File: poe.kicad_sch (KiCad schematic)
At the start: 57 parts, among them Q1 SI7430DP, Q2 MMBTA06LT1G, U1 MP8008, U10 MagJack-A70-112-331N126, U2 FOD817S, U3 750310744, U6 TL432DBZ, U7 TPD4EUSB30, U8 TPD4EUSB30

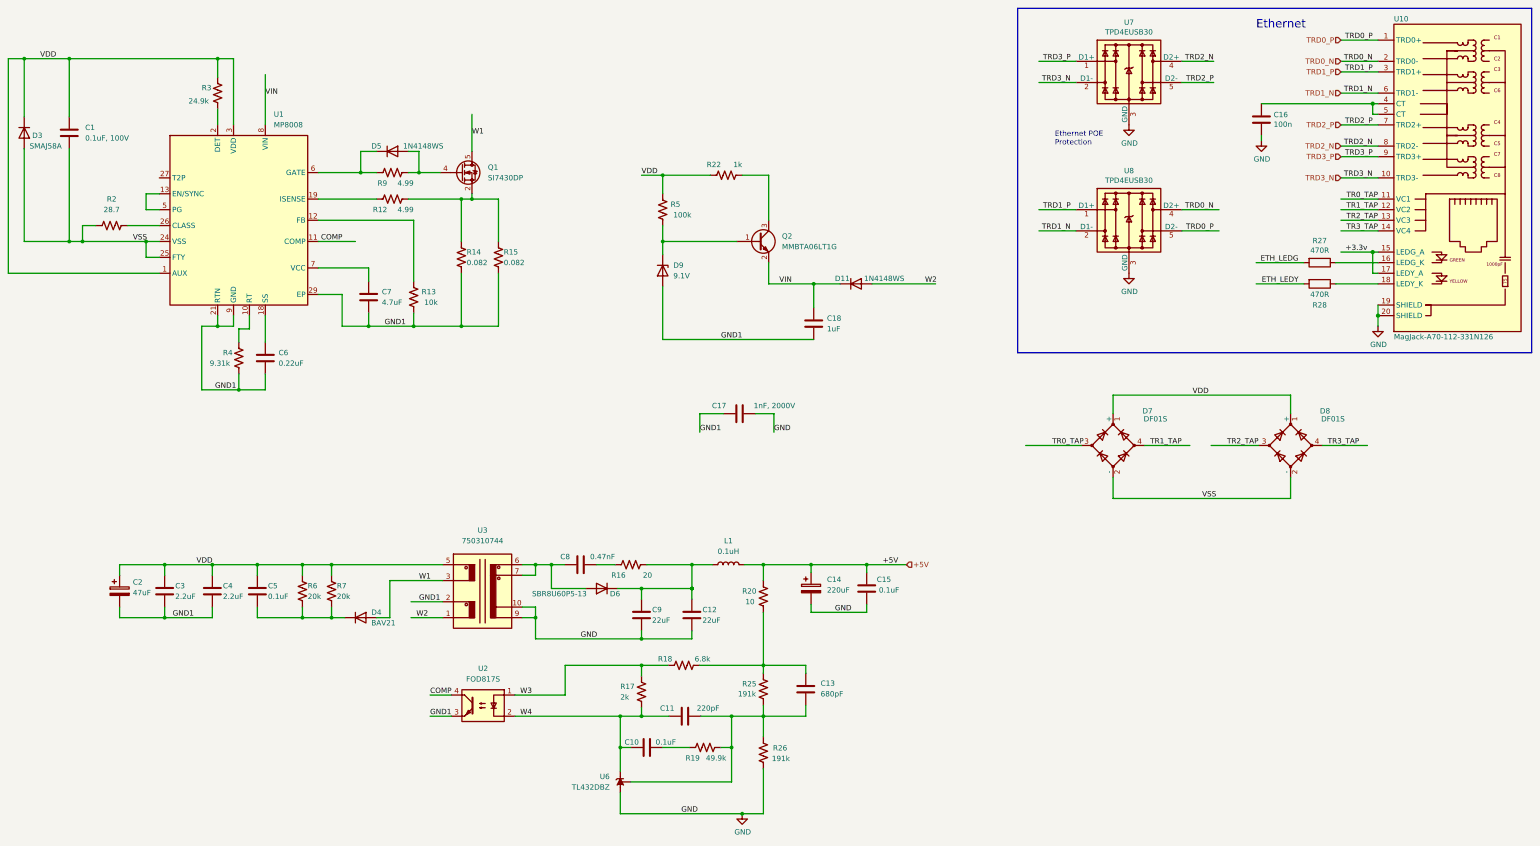
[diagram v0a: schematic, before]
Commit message: changed PoE transformer to Wurth 7491194912
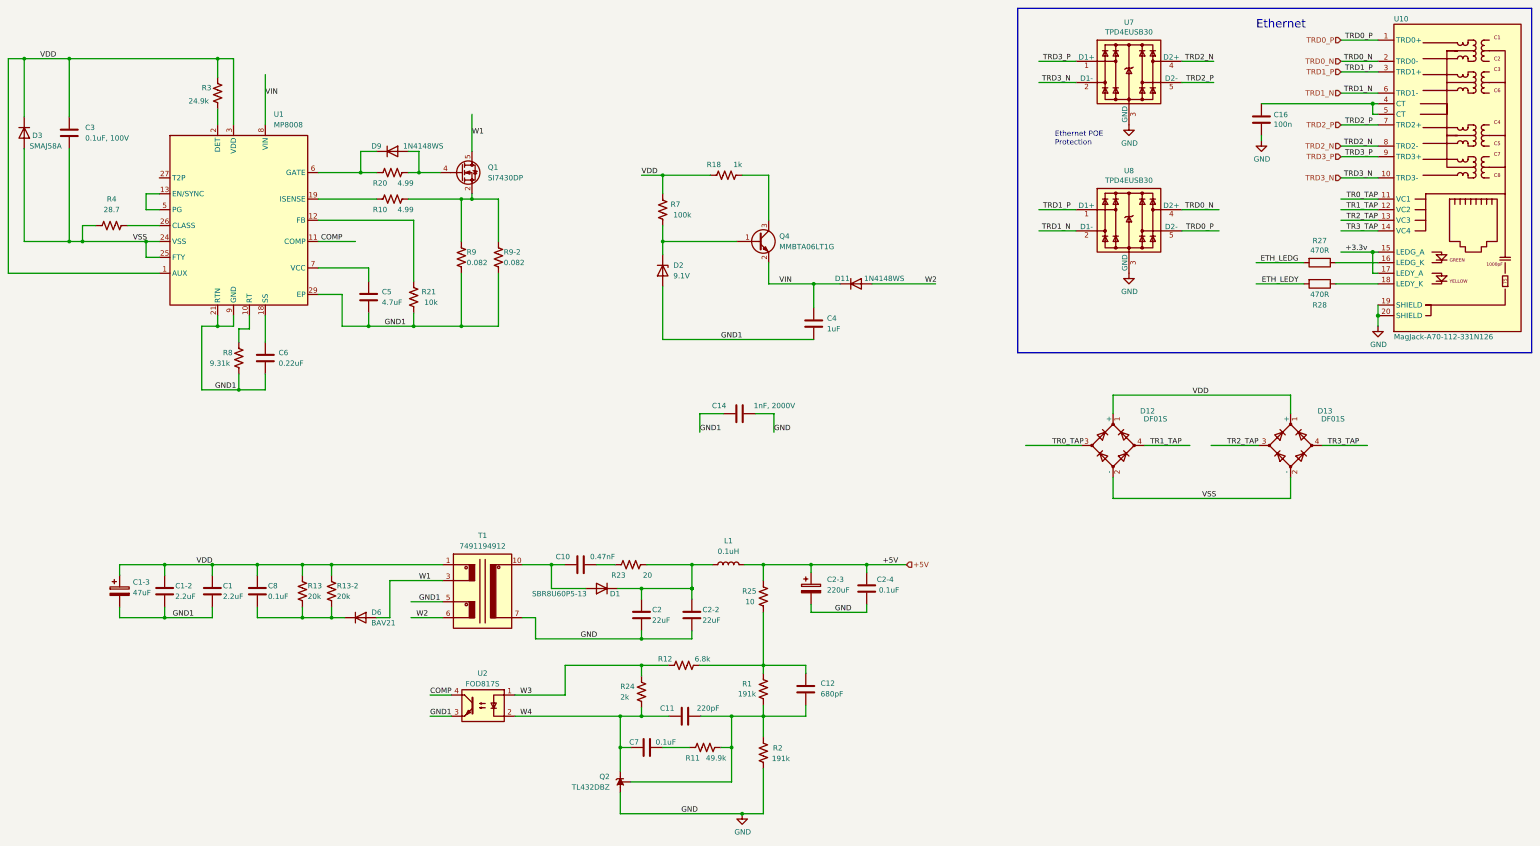
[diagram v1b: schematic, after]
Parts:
- T1: renamed from U3; value 750310744 -> 7491194912; footprint bitcart:750310744 -> bitcart:7491194912; symbol bitcart:750310744 -> bitcart:7491194912; DK (none) -> 732-2443-1-ND; ME 710-750310744 -> (none)
- renumbered C4 to C1, C3 to C1-2, C2 to C1-3, C8 to C10, C13 to C12, C17 to C14, C9 to C2, C12 to C2-2, C14 to C2-3, C15 to C2-4, C1 to C3, C18 to C4, C7 to C5, C10 to C7, C5 to C8, D6 to D1, D7 to D12, D8 to D13, D9 to D2, D4 to D6, D5 to D9, U6 to Q2, Q2 to Q4, R25 to R1, R12 to R10, R19 to R11, R18 to R12, R6 to R13, R7 to R13-2, R22 to R18, R26 to R2, R9 to R20, R13 to R21, R16 to R23, R17 to R24, R20 to R25, R2 to R4, R5 to R7, R4 to R8, R14 to R9, R15 to R9-2
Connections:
- net GND: now also T1.7, T1.8; no longer T1.10
- net GND1: now also T1.5; no longer T1.2
- net VDD: now also T1.1, T1.2; no longer T1.5
- net W1: now also T1.4
- net W2: now also T1.6; no longer T1.1
- net at C10.1, D1.2 (A), D1.3 (A): now also T1.10, T1.11, T1.12; no longer T1.6, T1.7

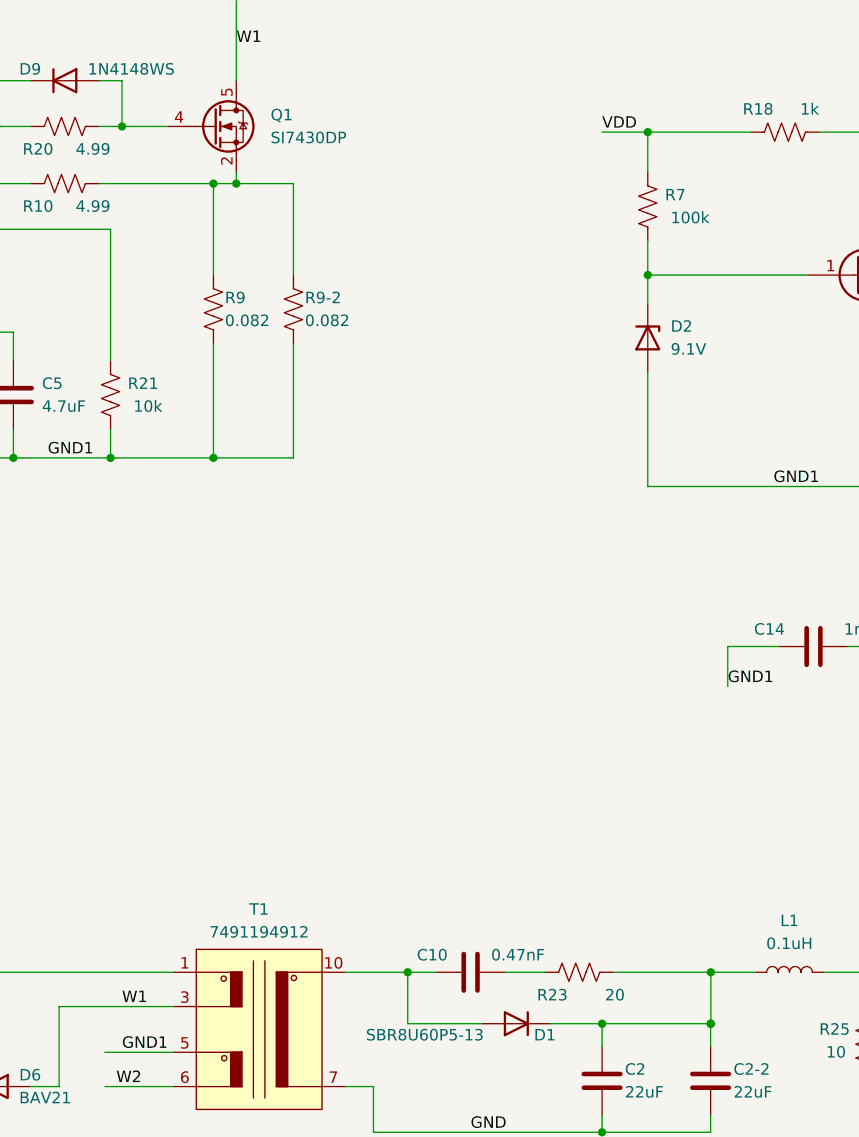
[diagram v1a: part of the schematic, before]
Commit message: started routing PoE
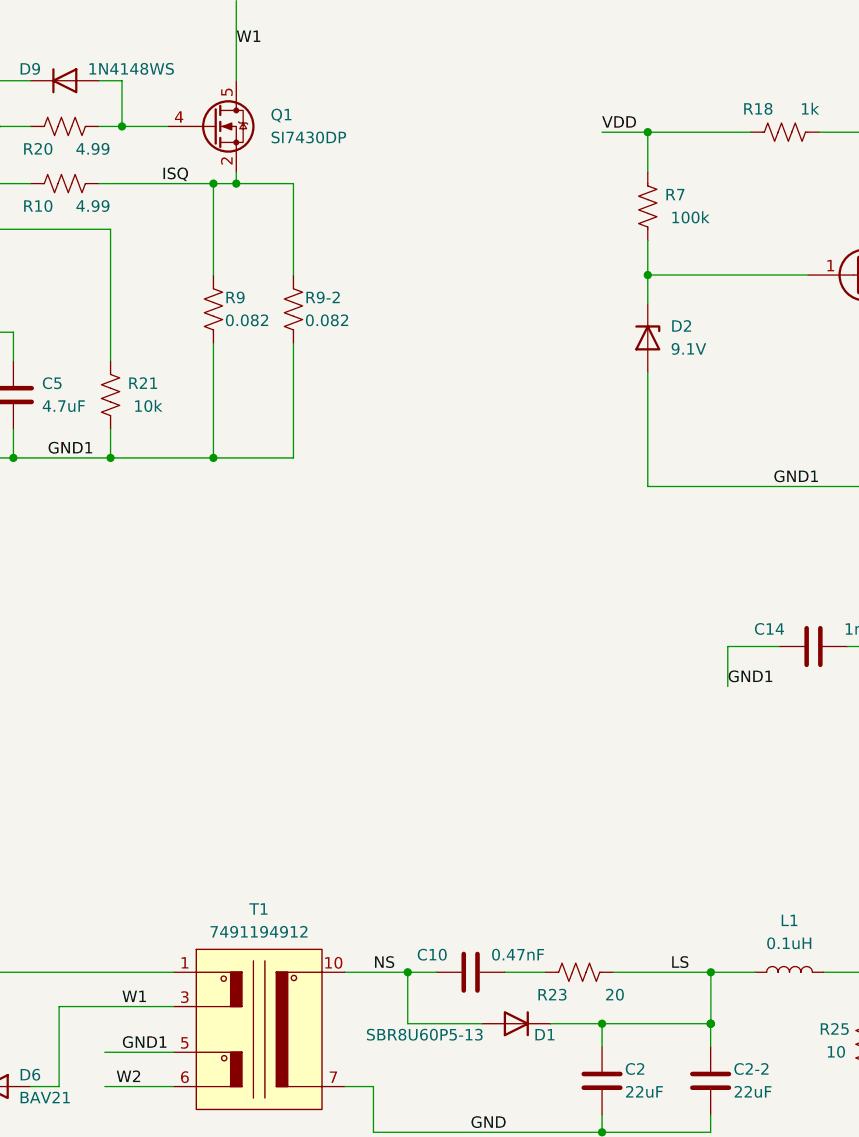
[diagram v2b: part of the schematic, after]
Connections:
- net ISQ: now reaches Q1.1 (S), Q1.2 (S), Q1.3 (S), R10.1, R9-2.2, R9.2
- net NS: now reaches C10.1, D1.2 (A), D1.3 (A), T1.10, T1.11, T1.12
- net LS: now reaches C2-2.1, C2.1, D1.1 (K), L1.1, R23.1
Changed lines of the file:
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@@
     (effects (font (size 1.27 1.27)) (justify right bottom))
+  )
+  (label "LS" (at 193.04 149.86 0)
+    (effects (font (size 1.27 1.27)) (justify left bottom))
   )
   (label "W4" (at 156.337 186.182 0)
@@
     (effects (font (size 1.27 1.27)) (justify right bottom))
   )
+  (label "ISQ" (at 136.525 62.23 0)
+    (effects (font (size 1.27 1.27)) (justify left bottom))
+  )
   (label "TRD3_P" (at 360.68 52.07 180)
     (effects (font (size 1.27 1.27)) (justify right bottom))
@@
     (effects (font (size 1.27 1.27)) (justify left bottom))
   )
+  (label "NS" (at 160.02 149.86 0)
+    (effects (font (size 1.27 1.27)) (justify left bottom))
+  )
